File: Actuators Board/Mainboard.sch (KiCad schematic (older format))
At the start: 78 parts, among them J1 USB_B_Micro, J10 Conn_01x02_Male, J12 Conn_01x02_Male, J2 8P8C_LED, J3 Micro_SD_Card_Det, J9 Conn_01x02_Male, Q1 MMDT2222A, Q3 PMV20ENR, U1 CP2102N-A01-GQFN24, U2 SN65HVD230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

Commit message: actually this time
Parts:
- removed BZ1: Buzzer, Buzzer_Beeper:Buzzer_TDK_PS1240P02BT_D12.2mm_H6.5mm, symbol Device:Buzzer
- removed D7: CABLE_DETECT, LED_SMD:LED_0603_1608Metric_Castellated, symbol Device:LED
- removed D8: D_Schottky, Diode_SMD:D_SOD-123F, symbol Device:D_Schottky
- removed J1: USB_B_Micro, Connector_USB:USB_Micro-B_Amphenol_10103594-0001LF_Horizontal, symbol Mainboard-rescue:USB_B_Micro-Connector
- removed J12: Conn_01x02_Male, Connector_PinHeader_2.54mm:PinHeader_1x02_P2.54mm_Vertical, symbol Connector:Conn_01x02_Male
- removed J2: 8P8C_LED, Connector_RJ:RJ45_Amphenol_RJHSE538X, symbol Connector:8P8C_LED
- removed J3: Micro_SD_Card_Det, Connector_Card:microSD_HC_Hirose_DM3AT-SF-PEJM5, symbol Connector:Micro_SD_Card_Det_Hirose_DM3AT
- removed JP1, JP5: SolderJumper_2_Open, Jumper:SolderJumper-2_P1.3mm_Open_TrianglePad1.0x1.5mm, symbol Jumper:SolderJumper_2_Open
- removed JP2: XBEE, iclr-hw:XBEE, symbol Mainboard-rescue:XBEE-iclr
- removed Q3: PMV20ENR, Package_TO_SOT_SMD:SOT-23, symbol Device:Q_NMOS_GSD
- removed R15, R18, R19: 470, Resistor_SMD:R_0603_1608Metric, symbol Device:R_Small
- removed R16, R17, R20, R23, R26, R31, R37, R38, R39, R40: 10K, Resistor_SMD:R_0603_1608Metric, symbol Device:R_Small
- removed TP1, TP24: TestPoint, TestPoint:TestPoint_THTPad_1.0x1.0mm_Drill0.5mm, symbol Connector:TestPoint
- removed U4: W25Q64FV, Package_SO:SOIC-8_3.9x4.9mm_P1.27mm, symbol Mainboard-rescue:W25Q64FV-iclr
- removed U5: MS5607-02BA, Package_LGA:LGA-8_3x5mm_P1.25mm, symbol Sensor_Pressure:MS5607-02BA
- added J?: USB_C_Receptacle_USB2.0, symbol Connector:USB_C_Receptacle_USB2.0
- added R?: 47.5k, symbol Device:R_Small
- added R?: 22.1k, symbol Device:R_Small
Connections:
- net labels added: Data+, Data-, VBUS
- wire segments 212 -> 128
- no-connect marks 40 -> 19
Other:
- moved on the sheet: D1, D9, R3, R4, R6, TP3, TP4, TP5, TP6, U1

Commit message: usbc completed and autoboot fixed
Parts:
- added R? (x2): 5.1k, symbol Device:R_Small
- C1, C2, C3: value 1nF -> 0.1uF
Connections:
- net GND: now also J?.A1 (GND), J?.A12 (GND), J?.B1 (GND), J?.B12 (GND), J?.S1 (SHIELD), R?.1, R?.2
- net at J?.A5 (CC1): now also R?.1
- net at J?.B5 (CC2): now also R?.2
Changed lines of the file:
@@
 P 900 7550
 F 0 "C2" V 671 7550 50  0000 C CNN
-F 1 "1nF" V 762 7550 50  0000 C CNN
+F 1 "0.1uF" V 762 7550 50  0000 C CNN
 F 2 "Capacitor_SMD:C_0603_1608Metric" H 900 7550 50  0001 C CNN
 F 3 "~" H 900 7550 50  0001 C CNN
@@
 P 2150 6700
 F 0 "C3" V 1921 6700 50  0000 C CNN
-F 1 "1nF" V 2012 6700 50  0000 C CNN
+F 1 "0.1uF" V 2012 6700 50  0000 C CNN
 F 2 "Capacitor_SMD:C_0603_1608Metric" H 2150 6700 50  0001 C CNN
 F 3 "~" H 2150 6700 50  0001 C CNN
@@
 P 1000 6700
 F 0 "C1" V 771 6700 50  0000 C CNN
-F 1 "1nF" V 862 6700 50  0000 C CNN
+F 1 "0.1uF" V 862 6700 50  0000 C CNN
 F 2 "Capacitor_SMD:C_0603_1608Metric" H 1000 6700 50  0001 C CNN
 F 3 "~" H 1000 6700 50  0001 C CNN
@@
 $EndComp
 $Comp
+L power:VDD #PWR053
+U 1 1 5E668CEC
+P 2200 2450
+F 0 "#PWR053" H 2200 2300 50  0001 C CNN
+F 1 "VDD" H 2217 2623 50  0000 C CNN
+F 2 "" H 2200 2450 50  0001 C CNN
+F 3 "" H 2200 2450 50  0001 C CNN
+	1    2200 2450
+	1    0    0    -1
+$EndComp
+Wire Wire Line
+	2200 3500 2200 2750
+$Comp
+L Connector:USB_C_Receptacle_USB2.0 J?
+U 1 1 6193041D
+P 1000 3350
+F 0 "J?" H 1107 4217 50  0000 C CNN
+F 1 "USB_C_Receptacle_USB2.0" H 1107 4126 50  0000 C CNN
+F 2 "" H 1150 3350 50  0001 C CNN
+F 3 "https://www.usb.org/sites/default/files/documents/usb_type-c.zip" H 1150 3350 50  0001 C CNN
+	1    1000 3350
+	1    0    0    -1
+$EndComp
+Wire Wire Line
+	1600 3450 1600 3550
+Wire Wire Line
+	1600 3550 1650 3550
+Connection ~ 1600 3550
+Text Label 1650 3550 0    50   ~ 0
+Data+
+Wire Wire Line
+	1600 3350 1600 3300
+Wire Wire Line
+	1600 3300 1650 3300
+Connection ~ 1600 3300
+Wire Wire Line
+	1600 3300 1600 3250
+Text Label 1650 3300 0    50   ~ 0
+Data-
+Text Label 2800 3900 2    50   ~ 0
+Data+
+Text Label 2800 4000 2    50   ~ 0
+Data-
+Wire Wire Line
+	2200 3500 2800 3500
+Text Label 2000 4350 1    50   ~ 0
+Data+
+Text Label 1900 4350 1    50   ~ 0
+Data-
+Text Label 1800 4350 1    50   ~ 0
+VBUS
+Connection ~ 2700 3800
+$Comp
+L Device:R_Small R?
+U 1 1 619CC6D3
+P 2300 4000
+F 0 "R?" H 2359 4046 50  0000 L CNN
+F 1 "47.5k" H 2359 3955 50  0000 L CNN
+F 2 "" H 2300 4000 50  0001 C CNN
+F 3 "~" H 2300 4000 50  0001 C CNN
+	1    2300 4000
+	1    0    0    -1
+$EndComp
+Wire Wire Line
+	2200 3800 2300 3800
+Wire Wire Line
+	2300 3900 2300 3800
+Connection ~ 2300 3800
+Wire Wire Line
+	2300 3800 2700 3800
+$Comp
+L power:GND #PWR?
+U 1 1 619E3CD1
+P 2300 4100
+F 0 "#PWR?" H 2300 3850 50  0001 C CNN
+F 1 "GND" H 2305 3927 50  0000 C CNN
+F 2 "" H 2300 4100 50  0001 C CNN
+F 3 "" H 2300 4100 50  0001 C CNN
+	1    2300 4100
+	1    0    0    -1
+$EndComp
+NoConn ~ 1600 3850
+NoConn ~ 1600 3950
+$Comp
+L Device:R_Small R?
+U 1 1 619F9DBD
+P 2100 3800
+F 0 "R?" V 1904 3800 50  0000 C CNN
+F 1 "22.1k" V 1995 3800 50  0000 C CNN
+F 2 "" H 2100 3800 50  0001 C CNN
+F 3 "~" H 2100 3800 50  0001 C CNN
+	1    2100 3800
+	0    1    1    0
+$EndComp
+Text Label 2000 3800 2    50   ~ 0
+VBUS
+Text Label 1600 2750 0    50   ~ 0
+VBUS
+Wire Wire Line
+	700  4250 850  4250
+$Comp
+L power:GND #PWR?
+U 1 1 618B804B
+P 850 4400
+F 0 "#PWR?" H 850 4150 50  0001 C CNN
+F 1 "GND" H 855 4227 50  0000 C CNN
+F 2 "" H 850 4400 50  0001 C CNN
+F 3 "" H 850 4400 50  0001 C CNN
+	1    850  4400
+	1    0    0    -1
+$EndComp
+Wire Wire Line
+	850  4250 850  4400
+Connection ~ 850  4250
+Wire Wire Line
+	850  4250 1000 4250
+Connection ~ 2200 2750
+$Comp
+L Device:R_Small R?
+U 1 1 618BE57C
+P 1900 2950
+F 0 "R?" V 2096 2950 50  0000 C CNN
+F 1 "5.1k" V 2005 2950 50  0000 C CNN
+F 2 "" H 1900 2950 50  0001 C CNN
+F 3 "~" H 1900 2950 50  0001 C CNN
+	1    1900 2950
+	0    -1   -1   0
+$EndComp
+$Comp
 L Device:D_Schottky D9
 U 1 1 5E667A26
@@
 	0    1    1    0
 $EndComp
-$Comp
-L power:VDD #PWR053
-U 1 1 5E668CEC
-P 2200 2450
-F 0 "#PWR053" H 2200 2300 50  0001 C CNN
-F 1 "VDD" H 2217 2623 50  0000 C CNN
-F 2 "" H 2200 2450 50  0001 C CNN
-F 3 "" H 2200 2450 50  0001 C CNN
-	1    2200 2450
-	1    0    0    -1
-$EndComp
-Wire Wire Line
-	2200 3500 2200 2750
-Connection ~ 2200 2750
-$Comp
-L Connector:USB_C_Receptacle_USB2.0 J?
-U 1 1 6193041D
-P 1000 3350
-F 0 "J?" H 1107 4217 50  0000 C CNN
-F 1 "USB_C_Receptacle_USB2.0" H 1107 4126 50  0000 C CNN
-F 2 "" H 1150 3350 50  0001 C CNN
-F 3 "https://www.usb.org/sites/default/files/documents/usb_type-c.zip" H 1150 3350 50  0001 C CNN
-	1    1000 3350
-	1    0    0    -1
-$EndComp
-Wire Wire Line
-	1600 3450 1600 3550
-Wire Wire Line
-	1600 3550 1650 3550
-Connection ~ 1600 3550
-Text Label 1650 3550 0    50   ~ 0
-Data+
-Wire Wire Line
-	1600 3350 1600 3300
-Wire Wire Line
-	1600 3300 1650 3300
-Connection ~ 1600 3300
-Wire Wire Line
-	1600 3300 1600 3250
-Text Label 1650 3300 0    50   ~ 0
-Data-
-Text Label 2800 3900 2    50   ~ 0
-Data+
-Text Label 2800 4000 2    50   ~ 0
-Data-
-Wire Wire Line
-	2200 3500 2800 3500
-Text Label 2000 4350 1    50   ~ 0
-Data+
-Text Label 1900 4350 1    50   ~ 0
-Data-
-Text Label 1800 4350 1    50   ~ 0
-VBUS
-Connection ~ 2700 3800
+Wire Wire Line
+	1600 2950 1800 2950
 $Comp
 L Device:R_Small R?
-U 1 1 619CC6D3
-P 2300 4000
-F 0 "R?" H 2359 4046 50  0000 L CNN
-F 1 "47.5k" H 2359 3955 50  0000 L CNN
-F 2 "" H 2300 4000 50  0001 C CNN
-F 3 "~" H 2300 4000 50  0001 C CNN
-	1    2300 4000
-	1    0    0    -1
-$EndComp
-Wire Wire Line
-	2200 3800 2300 3800
-Wire Wire Line
-	2300 3900 2300 3800
-Connection ~ 2300 3800
-Wire Wire Line
-	2300 3800 2700 3800
+U 1 1 618E53EA
+P 1900 3150
+F 0 "R?" V 1704 3150 50  0000 C CNN
+F 1 "5.1k" V 1795 3150 50  0000 C CNN
+F 2 "" H 1900 3150 50  0001 C CNN
+F 3 "~" H 1900 3150 50  0001 C CNN
+	1    1900 3150
+	0    1    1    0
+$EndComp
+Wire Wire Line
+	1600 3050 1700 3050
+Wire Wire Line
+	1700 3050 1700 3150
+Wire Wire Line
+	1700 3150 1800 3150
 $Comp
 L power:GND #PWR?
-U 1 1 619E3CD1
-P 2300 4100
-F 0 "#PWR?" H 2300 3850 50  0001 C CNN
-F 1 "GND" H 2305 3927 50  0000 C CNN
-F 2 "" H 2300 4100 50  0001 C CNN
-F 3 "" H 2300 4100 50  0001 C CNN
-	1    2300 4100
-	1    0    0    -1
-$EndComp
-NoConn ~ 1600 3850
-NoConn ~ 1600 3950
-$Comp
-L Device:R_Small R?
-U 1 1 619F9DBD
-P 2100 3800
-F 0 "R?" V 1904 3800 50  0000 C CNN
-F 1 "22.1k" V 1995 3800 50  0000 C CNN
-F 2 "" H 2100 3800 50  0001 C CNN
-F 3 "~" H 2100 3800 50  0001 C CNN
-	1    2100 3800
-	0    1    1    0
-$EndComp
-Text Label 2000 3800 2    50   ~ 0
-VBUS
-Text Label 1600 2750 0    50   ~ 0
-VBUS
+U 1 1 618ECFF5
+P 2050 3050
+F 0 "#PWR?" H 2050 2800 50  0001 C CNN
+F 1 "GND" V 2055 2922 50  0000 R CNN
+F 2 "" H 2050 3050 50  0001 C CNN
+F 3 "" H 2050 3050 50  0001 C CNN
+	1    2050 3050
+	0    -1   -1   0
+$EndComp
+Wire Wire Line
+	2000 3150 2000 3050
+Wire Wire Line
+	2000 3050 2050 3050
+Wire Wire Line
+	2000 2950 2000 3050
+Connection ~ 2000 3050
 $EndSCHEMATC

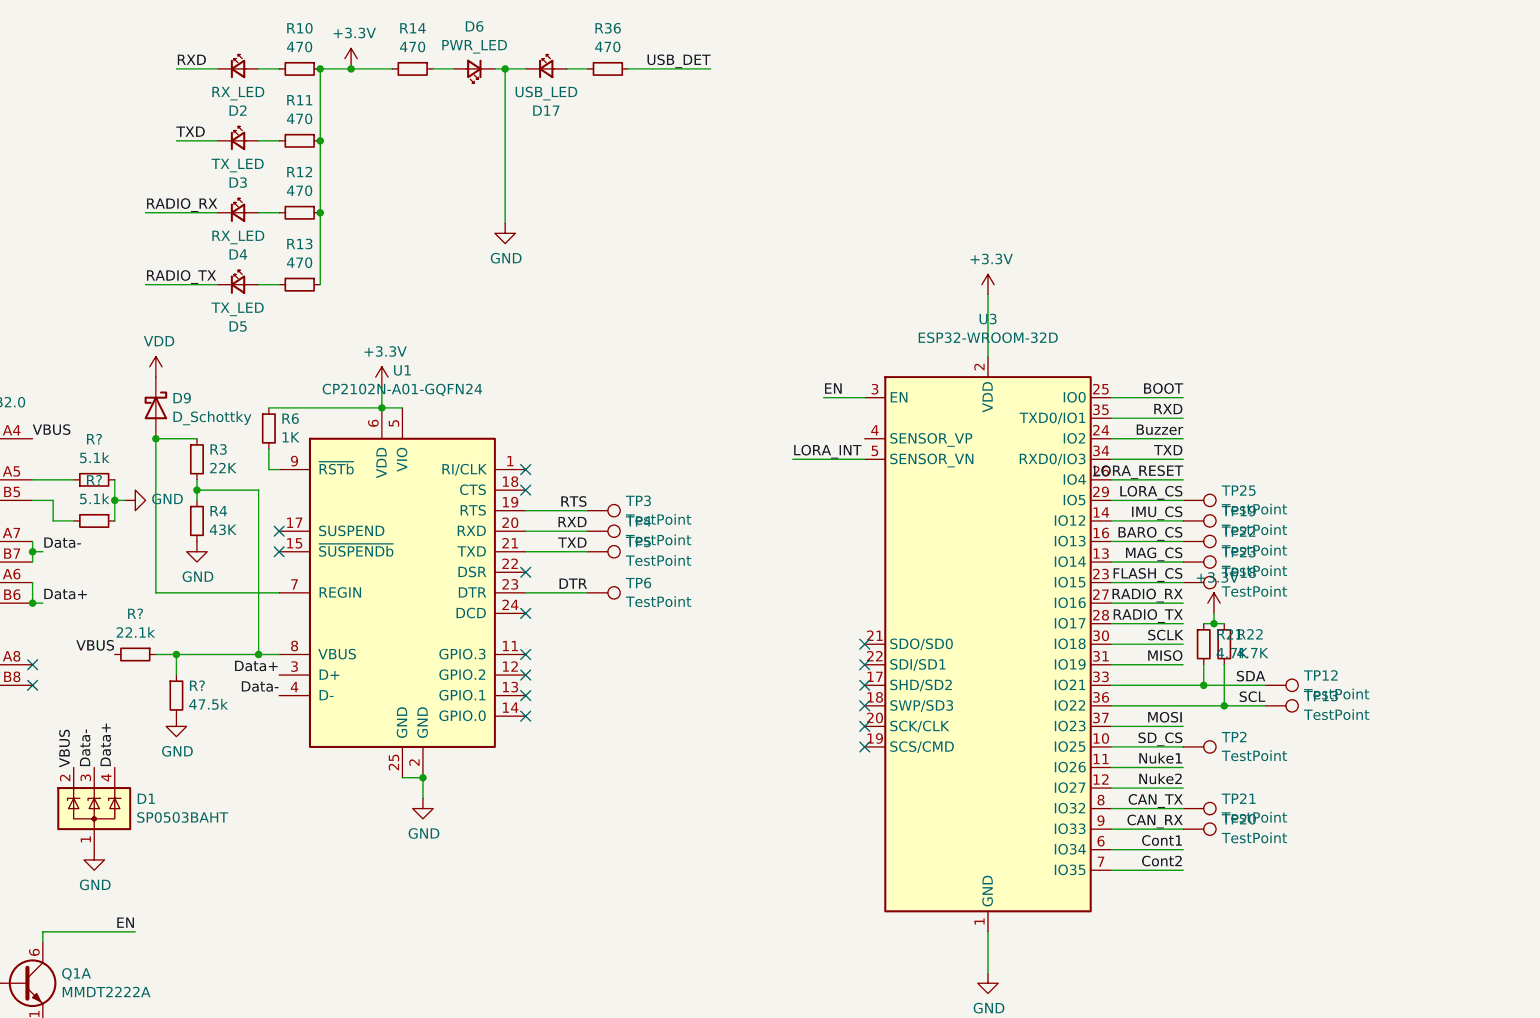
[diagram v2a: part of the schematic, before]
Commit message: (hopefully) last unnecessary nets removed
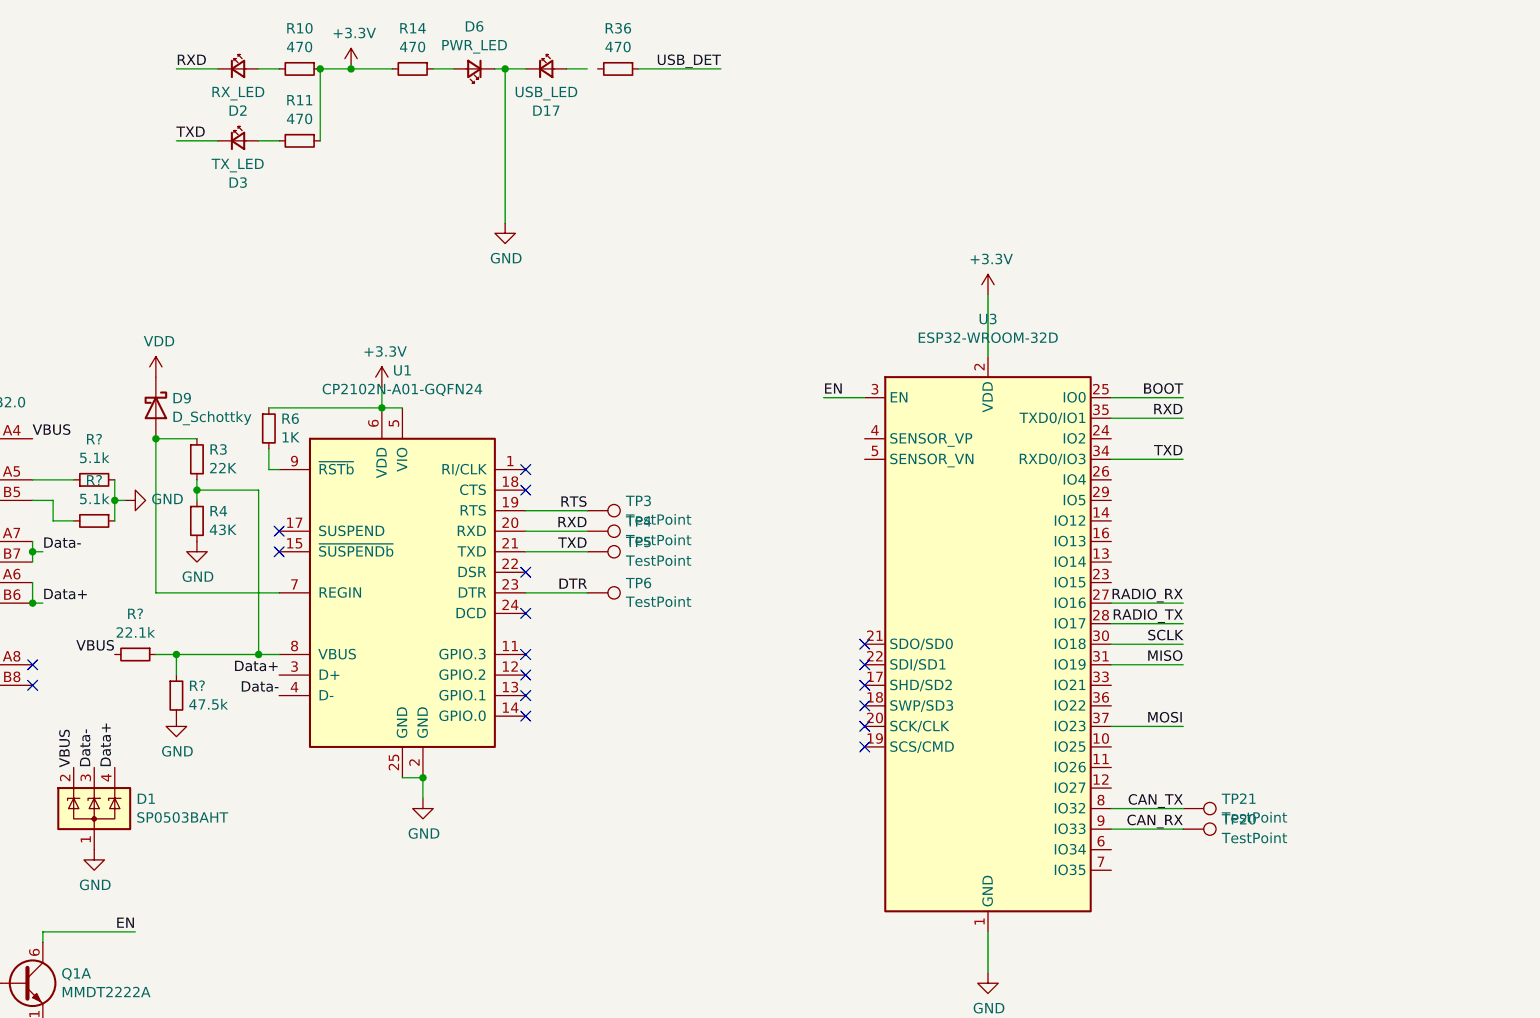
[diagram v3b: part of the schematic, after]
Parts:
- removed D4: RX_LED, LED_SMD:LED_0603_1608Metric_Castellated, symbol Device:LED_Small
- removed D5: TX_LED, LED_SMD:LED_0603_1608Metric_Castellated, symbol Device:LED_Small
- removed R12, R13: 470, Resistor_SMD:R_0603_1608Metric, symbol Device:R_Small
- removed R21, R22: 4.7K, Resistor_SMD:R_0603_1608Metric, symbol Device:R_Small
- removed TP12, TP13, TP18, TP19, TP2, TP22, TP23, TP25: TestPoint, TestPoint:TestPoint_THTPad_1.0x1.0mm_Drill0.5mm, symbol Connector:TestPoint
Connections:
- net at D17.2 (A): no longer R36.2
- net BARO_CS: no longer names the net of U3.16 (IO13)
- net Buzzer: no longer names the net of U3.24 (IO2)
- net Cont1: no longer names the net of U3.6 (IO34)
- net Cont2: no longer names the net of U3.7 (IO35)
- net FLASH_CS: no longer names the net of U3.23 (IO15)
- net IMU_CS: no longer names the net of U3.14 (IO12)
- net LORA_CS: no longer names the net of U3.29 (IO5)
- net LORA_INT: no longer names the net of U3.5 (SENSOR_VN)
- net LORA_RESET: no longer names the net of U3.26 (IO4)
- net MAG_CS: no longer names the net of U3.13 (IO14)
- net Nuke1: no longer names the net of U3.11 (IO26)
- net Nuke2: no longer names the net of U3.12 (IO27)
- net SCL: no longer names the net of U3.36 (IO22)
- net SDA: no longer names the net of U3.33 (IO21)
- net SD_CS: no longer names the net of U3.10 (IO25)
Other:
- moved on the sheet: R36
